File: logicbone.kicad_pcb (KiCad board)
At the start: 8 copper layers, 86.4 x 54.6 mm, 253 parts, among them IC1 ECP5UM-CABGA381, IC10 AT25SL128A, IC11 FAN5362UMP, IC12 74LVC1G07, IC13 TPS51206, IC14 KSZ9031RNXCA, IC15 TC7USB40MU, IC16 NCP349, IC17 NCP110AMX110, IC18 NCP110AMX110, IC19 NCP115AMX250, IC2 DDR3-TFBGA78, IC20 NCP115AMX250, IC3 DDR3-TFBGA78, IC4 MXL7704, IC5 PI6CG18401, IC6 74LVC1G02, IC7 FUSB302-QFN14, IC8 STM32FLxx-QFN48, IC9 ADC120, J1 NGFF-KEY-E, J2 GCT_USB4110_USBC, J3 ARJM11xx-502, J4 FTSH-105-DV-K, J5 Conn_02x05_Odd_Even, J6 Micro_SD_MEM2075, P8 BB_2x23, P9 BB_2x23, Q1 Q_PMOS_GSD, SW1 SW_SPST, SW2 SW_SPST, Y1 25MHz, Y2 32.768kHz

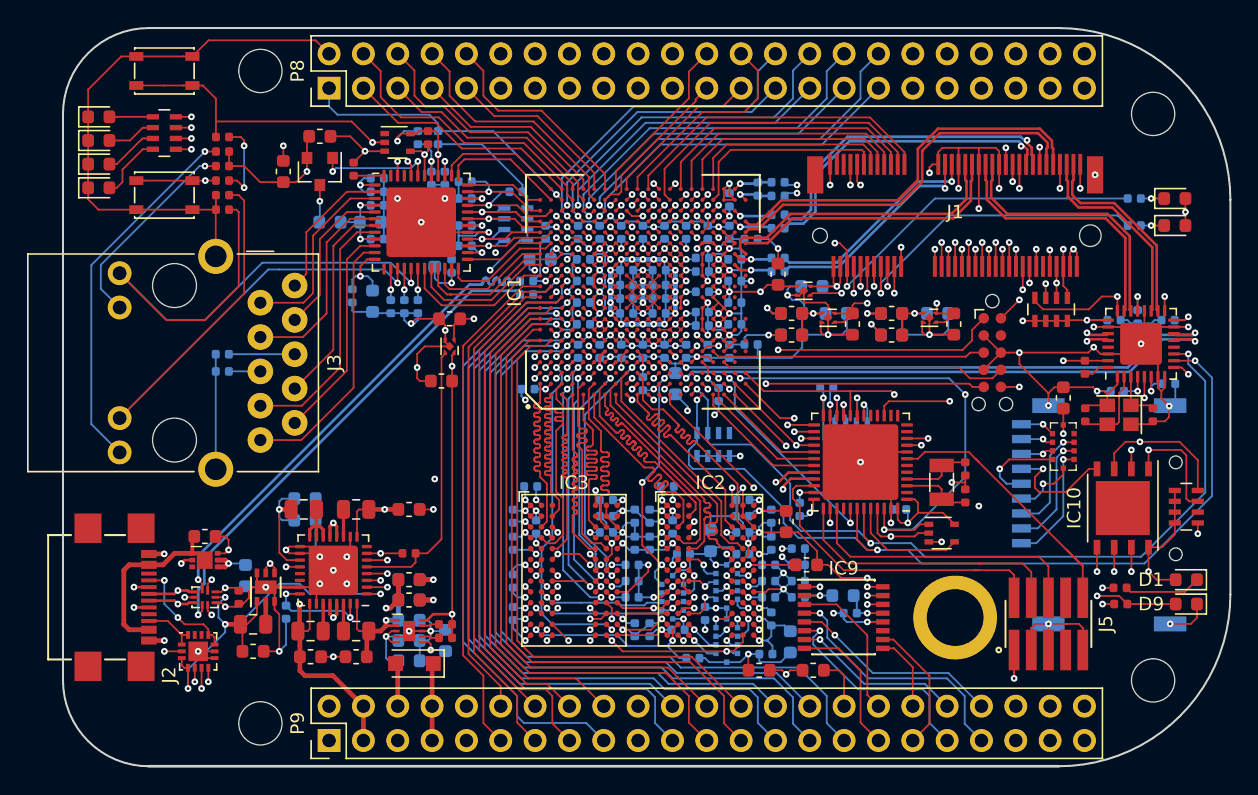
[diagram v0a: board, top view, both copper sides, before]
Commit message: Move +3V3 supply onto PMIC LDO.
The default configuration of the MXL7704 allows the LDO to be used
as an always-on supply by controlling the power-on using SEQ_EN in
place of GLOBAL_EN. Doing so allows us to elminiate another
regulator.
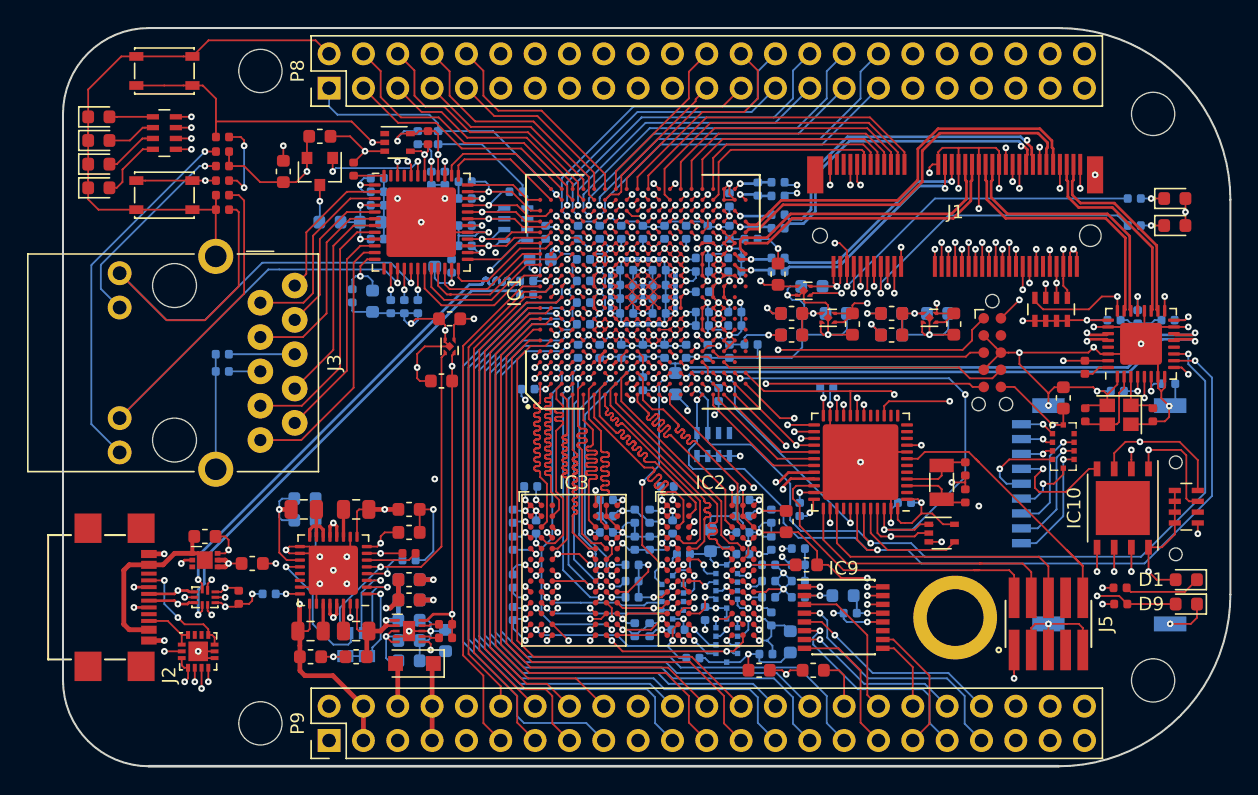
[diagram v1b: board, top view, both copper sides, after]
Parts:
- removed IC11: FAN5362UMP, Package_DFN_QFN:DFN-6-1EP_2x2mm_P0.65mm_EP1x1.6mm
- removed L12: L, Inductor_SMD:L_0805_2012Metric
- added R32: 10k, Resistor_SMD:R_0402_1005Metric, B.Cu at (125.6, 84.8)
- C104: moved to F.Cu
- moved RN8 39.8 mm to (121.7, 91.0)
- moved C100 14.5 mm to (125.6, 82.7)
- moved C107 1.84 mm to (115.2, 87.2), turned to 180 degrees
- moved C104 1.03 mm to (114.0, 85.0), turned to 0 degrees
- moved C517 0.70 mm to (149.7, 66.4)
- moved C516 0.70 mm to (149.7, 63.4)
- moved C103 0.61 mm to (162.2, 80.5)
- moved C252 0.10 mm to (149.7, 67.4)
- moved C258 0.10 mm to (149.7, 62.4)
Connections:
- C280 pad 1: +3V3 -> VCC3V3
- C281 pad 1: +3V3 -> VCC3V3
- D1 pad 2: +3V3 -> VCC3V3
- IC1 pad D10: /Exp Headers/P9_GPIO21 -> /Exp Headers/ADC_SCLK
- IC1 pad D9: /Exp Headers/ADC_SCLK -> /Exp Headers/P9_GPIO21
- IC1 pad P10: +3V3 -> VCC3V3
- IC1 pad P9: +3V3 -> VCC3V3
- IC1 pad T4: +3V3 -> VCC3V3
- IC10 pad 8: +3V3 -> VCC3V3
- IC4 pad 7: +3V3 -> VBUS
- IC4 pad 8: Net-(IC4-Pad8) -> +3V3
- IC8 pad 10: /Supervisor/PMIC_ENABLE -> Net-(IC8-Pad10)
- J4 pad 6: +3V3 -> VCC3V3
- R17 pad 2: +3V3 -> VCC3V3
- R18 pad 1: /FPGA Power/PWR_VCCAUX -> /Supervisor/PMIC_ENABLE
- R18 pad 2: +3V3 -> VBUS
- RN7 pad 5: +3V3 -> VCC3V3
- RN7 pad 6: +3V3 -> VCC3V3
- RN7 pad 7: +3V3 -> VCC3V3
- RN7 pad 8: +3V3 -> VCC3V3
- RN8 pad 1: /Supervisor/PMIC_SDA -> /FPGA Power/PWR_VCCAUX
- RN8 pad 2: /Supervisor/PMIC_SCL -> /Supervisor/PMIC_PGOOD
- RN8 pad 3: /Supervisor/PMIC_PGOOD -> /Supervisor/PMIC_SCL
- RN8 pad 4: /Supervisor/PMIC_SEQ -> /Supervisor/PMIC_SDA
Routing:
- net +3V3: track 245.5 -> 183.8 mm, vias 18 -> 12
- net /Supervisor/PMIC_ENABLE: track 60.3 -> 3.82 mm, vias 2 -> 0
- net VCC3V3: track 371.9 -> 416.4 mm, vias 22 -> 26
- net GND: track 1317.7 -> 1337.2 mm, vias 147 -> 146
- net /Supervisor/PMIC_PGOOD: track 52.3 -> 59.6 mm
- net /FPGA Power/PWR_VCCAUX: track 20.6 -> 26.7 mm, vias 0 -> 1
- net VBUS: track 50.4 -> 54.7 mm
- net /Supervisor/PMIC_SCL: track 52.7 -> 55.8 mm
- net /FPGA Power/VCCA1: track 17.1 -> 19.4 mm
- net /Supervisor/PMIC_SDA: track 51.9 -> 54.2 mm
- net Net-(IC11-Pad2): track 1.70 -> 0.00 mm
- net /FPGA SERDES/VCCTRX1: track 26.1 -> 24.9 mm
- net /Exp Headers/ADC_SCLK: track 40.7 -> 40.3 mm, vias 3 -> 2
- net VCCAUXTRX: track 16.4 -> 16.5 mm, vias 3 -> 4

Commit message: Remove STM32 and plan to use an FPGA bootloader instead.
The MXL7704 is close enough to what the ECP5 needs that we can let
it boot itself from the OTP and then fixup the voltages once the
FPGA bootloader starts (the OTP is correct for the ECP5-5G).
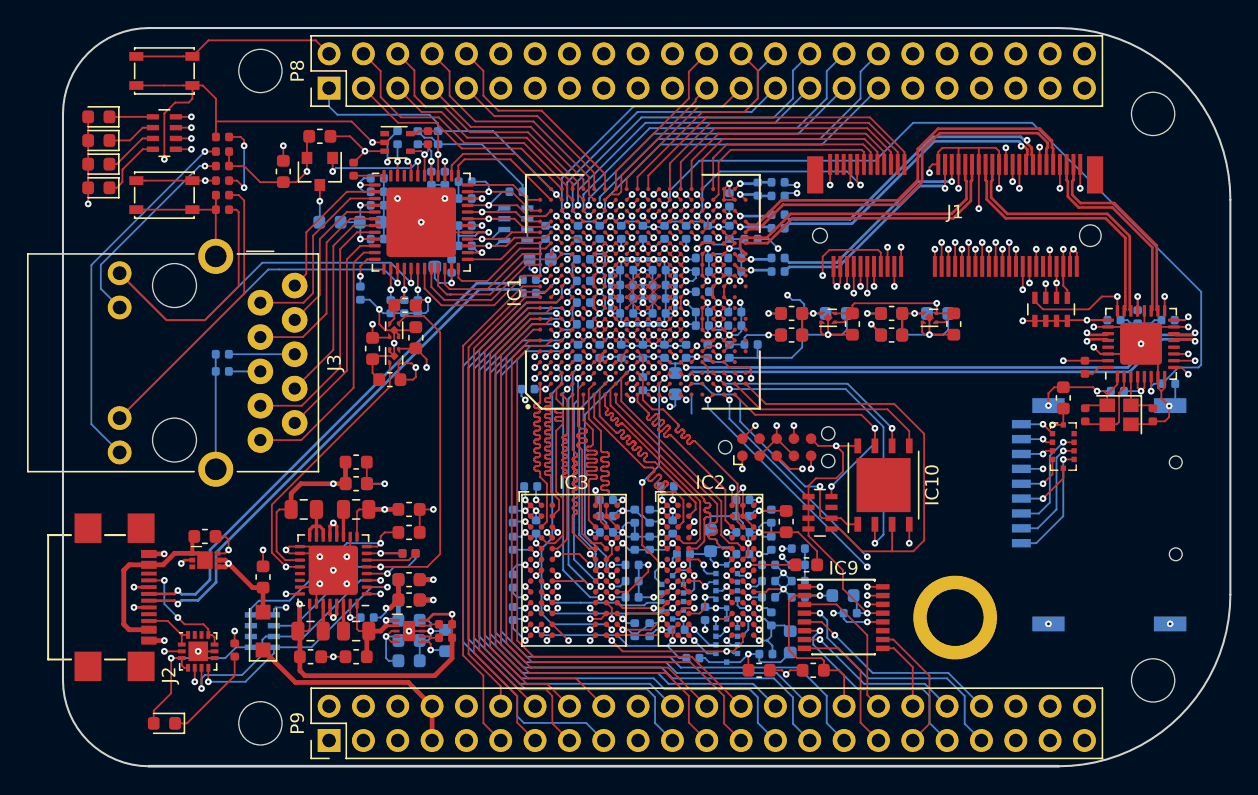
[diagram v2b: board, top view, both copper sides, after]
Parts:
- removed C101, C102, C103, C281: 100nF, Capacitor_SMD:C_0402_1005Metric
- removed C105, C106, C107: C_Small, Capacitor_SMD:C_0402_1005Metric
- removed D7, D8, D9: LED_ALT, LED_SMD:LED_0603_1608Metric
- removed IC15: TC7USB40MU, Package_DFN_QFN:UQFN-10_1.4x1.8mm_P0.4mm
- removed IC6: 74LVC1G02, Package_TO_SOT_SMD:SOT-353_SC-70-5
- removed IC8: STM32FLxx-QFN48, Package_DFN_QFN:QFN-48-1EP_7x7mm_P0.5mm_EP5.6x5.6mm
- removed J5: Conn_02x05_Odd_Even, KiCAD_Magic:ftsh-105-01-dv
- removed R11, R12: 10k, Resistor_SMD:R_0402_1005Metric
- removed R17: 470, Resistor_SMD:R_0402_1005Metric
- removed R34: 4.7k, Resistor_SMD:R_0402_1005Metric
- removed RN8: 4.7k, Resistor_SMD:R_Array_Concave_4x0603
- removed Y2: 32.768kHz, Crystal:Crystal_SMD_3215-2Pin_3.2x1.5mm
- added C1: C_Small, Capacitor_SMD:C_0402_1005Metric, B.Cu at (122.5, 89.0)
- added C2: 100nF, Capacitor_SMD:C_0402_1005Metric, B.Cu at (124.8, 53.5)
- C152, C161, C304, R32: moved to F.Cu
- J4: value FTSH-105-DV-K -> TC2050-IDC-NL
- R18: moved to B.Cu
- moved D1 76.3 mm to (107.5, 96.8)
- moved R10 65.7 mm to (112.7, 91.4), turned to 270 degrees
- moved RN5 36.1 mm to (114.8, 90.0), turned to 180 degrees
- moved C161 32.0 mm to (124.2, 71.4)
- moved C167 30.5 mm to (122.9, 69.1), turned to 270 degrees
- moved IC19 30.4 mm to (124.5, 67.8), turned to 90 degrees
- moved RN7 27.1 mm to (156.0, 81.2)
- moved IC10 17.8 mm to (160.7, 79.2), turned to 90 degrees
- moved J4 17.4 mm to (152.8, 76.4), turned to 0 degrees
- moved D6 11.5 mm to (114.8, 90.0), turned to 90 degrees
- moved C162 9.88 mm to (121.7, 79.1), turned to 0 degrees
- moved C280 7.69 mm to (147.3, 64.9), turned to 0 degrees
- moved C151 4.66 mm to (121.7, 79.1)
- moved C152 4.65 mm to (121.7, 77.5)
- moved IC20 4.16 mm to (124.5, 69.7)
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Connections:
- net /FPGA SERDES/M2_USB_DM renamed /FPGA SERDES/M2_USB-
- net /FPGA SERDES/M2_USB_DP renamed /FPGA SERDES/M2_USB+
- net /Supervisor/FLASH_MISO renamed /FPGA Programming/FLASH_MISO
- net /Supervisor/FLASH_MOSI renamed /FPGA Programming/FLASH_MOSI
- net /Supervisor/FLASH_SCLK renamed /FPGA Programming/FLASH_SCLK
- net /Supervisor/FPGA_TCK renamed /FPGA Programming/FPGA_TCK
- net /Supervisor/FPGA_TDI renamed /FPGA Programming/FPGA_TDI
- net /Supervisor/FPGA_TDO renamed /FPGA Programming/FPGA_TDO
- net /Supervisor/FPGA_TMS renamed /FPGA Programming/FPGA_TMS
- net /Supervisor/USB_CC1 renamed /FPGA Programming/USB_CC1
- net /Supervisor/USB_CC2 renamed /FPGA Programming/USB_CC2
- net /Supervisor/~FPGA_INIT renamed /FPGA Programming/~FPGA_INIT
- C162 pad 1: VCC3V3 -> VCORE
- D1 pad 2: VCC3V3 -> +3V3
- D2 pad 1: GND -> Net-(D2-Pad1)
- D2 pad 2: Net-(D2-Pad2) -> VCC3V3
- D3 pad 1: GND -> Net-(D3-Pad1)
- D3 pad 2: Net-(D3-Pad2) -> VCC3V3
- D4 pad 1: GND -> Net-(D4-Pad1)
- D4 pad 2: Net-(D4-Pad2) -> VCC3V3
- D5 pad 1: GND -> Net-(D5-Pad1)
- D5 pad 2: Net-(D5-Pad2) -> VCC3V3
- IC1 pad D13: /Ethernet/MMC_DAT0 -> /Ethernet/MMC_DAT2
- IC1 pad E13: /Ethernet/MMC_DAT2 -> /Ethernet/MMC_DAT0
- IC1 pad E14: /Ethernet/MMC_DET -> /Ethernet/MMC_CMD
- IC1 pad E15: /Ethernet/MMC_CMD -> /Ethernet/MMC_DET
- IC1 pad L16: /FPGA SERDES/~M2_WDIS2 -> /FPGA SERDES/M2_SUSCLK
- IC1 pad L17: /FPGA SERDES/~PCIE_RESET0 -> /FPGA SERDES/~M2_WDIS2
- IC1 pad L18: /FPGA SERDES/~PCIE_RESET1 -> /FPGA SERDES/~PCIE_WAKE0
- IC1 pad M18: /FPGA SERDES/M2_SUSCLK -> /FPGA SERDES/~PCIE_RESET0
- IC1 pad M19: /FPGA SERDES/~PCIE_WAKE0 -> /Ethernet/25M_REFCLK
- IC1 pad N1: /FPGA Memory/~DDR3_RST -> Net-(IC1-PadN1)
- IC1 pad N17: /FPGA SERDES/M2_COEX2 -> /FPGA SERDES/M2_COEX3
- IC1 pad N18: /FPGA SERDES/M2_VEND1 -> /FPGA SERDES/M2_VEND2
- IC1 pad N19: /FPGA SERDES/~M2_SDIO_WAKE -> /FPGA SERDES/~PCIE_RESET1
- IC1 pad N20: /FPGA SERDES/M2_COEX3 -> /FPGA SERDES/~M2_SDIO_WAKE
- IC1 pad P1: Net-(IC1-PadP1) -> /FPGA Memory/~DDR3_RST
- IC1 pad P18: /FPGA SERDES/M2_COEX1 -> /FPGA SERDES/M2_COEX2
- IC1 pad P19: /FPGA SERDES/M2_VEND2 -> /FPGA SERDES/M2_VEND1
- IC1 pad R1: /Exp Headers/SDA -> Net-(IC1-PadR1)
- IC1 pad R16: /FPGA SERDES/M2_TXD -> Net-(IC1-PadR16)
- IC1 pad R17: /FPGA SERDES/M2_RXD -> /FPGA SERDES/M2_TXD
- IC1 pad R2: /Supervisor/~FLASH_CSEL -> /FPGA Programming/~FLASH_CSEL
- IC1 pad R3: /Supervisor/USB_SEL -> /FPGA Programming/~USB_INT
- IC1 pad T1: /Exp Headers/SCL -> Net-(IC1-PadT1)
- IC1 pad T19: /FPGA SERDES/M2_VEND0 -> /FPGA SERDES/M2_COEX1
- IC1 pad T2: /Exp Headers/PWR_BUTTON -> Net-(IC1-PadT2)
- IC1 pad U1: /Supervisor/FPGA_UART_RXD -> /Exp Headers/SCL
- IC1 pad U17: /FPGA SERDES/M2_LED1 -> /FPGA SERDES/M2_RXD
- IC1 pad U18: /FPGA SERDES/M2_LED2 -> /FPGA SERDES/M2_VEND0
- IC1 pad U2: /Supervisor/FPGA_UART_TXD -> /Exp Headers/PWR_BUTTON
- IC1 pad V1: /Supervisor/FPGA_UART_CLK -> /Exp Headers/SDA
- IC1 pad W1: /Supervisor/FLASH_D3 -> /FPGA Programming/FLASH_D3
- IC1 pad Y2: /Supervisor/FLASH_D2 -> /FPGA Programming/FLASH_D2
- IC1 pad Y3: /Supervisor/FPGA_DONE -> /FPGA Programming/FPGA_DONE
- IC10 pad 1: /Supervisor/~FLASH_CSEL -> /FPGA Programming/~FLASH_CSEL
- IC10 pad 3: /Supervisor/FLASH_D2 -> /FPGA Programming/FLASH_D2
- IC10 pad 7: /Supervisor/FLASH_D3 -> /FPGA Programming/FLASH_D3
- IC14 pad 46: /Ethernet/25M_REFCLK -> Net-(C2-Pad2)
- IC19 pad 3: /FPGA Power/PWR_SERDES -> /FPGA Power/PMIC_PG1
- IC20 pad 3: /FPGA Power/PWR_VCCAUX -> /FPGA Power/PMIC_PG2
- IC4 pad 2: /Supervisor/PMIC_SDA -> /Exp Headers/SDA
- IC4 pad 20: /Supervisor/PMIC_PGOOD -> /FPGA Power/PMIC_PG2
- IC4 pad 3: /Supervisor/PMIC_SCL -> /Exp Headers/SCL
- IC4 pad 4: /Supervisor/PMIC_SEQ -> /FPGA Power/PMIC_SEQ
- IC4 pad 5: /FPGA Power/PWR_VCCAUX -> /FPGA Power/PMIC_PG1
- IC4 pad 6: /Supervisor/PMIC_ENABLE -> /FPGA Power/PMIC_ENABLE
- IC5 pad 5: VCC3V3 -> VCC1V8
- IC7 pad 5: /Supervisor/~USB_INT -> /FPGA Programming/~USB_INT
- J1 pad 16: /FPGA SERDES/M2_LED2 -> /Ethernet/LED_USER2
- J1 pad 6: /FPGA SERDES/M2_LED1 -> /Ethernet/LED_USER1
- J2 pad A6: /Supervisor/USB_D+ -> /Ethernet/FPGA_USB+
- J2 pad A7: /Supervisor/USB_D- -> /Ethernet/FPGA_USB-
- J2 pad B6: /Supervisor/USB_D+ -> /Ethernet/FPGA_USB+
- J2 pad B7: /Supervisor/USB_D- -> /Ethernet/FPGA_USB-
- R1 pad 1: Net-(IC1-PadB12) -> /Ethernet/FPGA_USB+
- R1 pad 2: /Ethernet/FPGA_USB+ -> Net-(IC1-PadB12)
- R18 pad 1: /Supervisor/PMIC_ENABLE -> VBUS
- R18 pad 2: VBUS -> /FPGA Power/PMIC_SEQ
- R2 pad 1: Net-(IC1-PadC12) -> /Ethernet/FPGA_USB-
- R2 pad 2: /Ethernet/FPGA_USB- -> Net-(IC1-PadC12)
- R32 pad 1: GND -> /FPGA Power/PMIC_ENABLE
- R32 pad 2: /Supervisor/PMIC_SEQ -> VBUS
- RN5 pad 1: /Exp Headers/SCL -> /FPGA Power/PMIC_PG2
- RN5 pad 2: /Exp Headers/SDA -> /FPGA Power/PMIC_PG1
- RN5 pad 3: Net-(RN5-Pad3) -> /Exp Headers/SCL
- RN5 pad 4: Net-(RN5-Pad4) -> /Exp Headers/SDA
- RN7 pad 1: /Supervisor/FLASH_D3 -> /FPGA Programming/FLASH_D2
- RN7 pad 2: Net-(RN7-Pad2) -> /FPGA Programming/~FLASH_CSEL
- RN7 pad 3: /Supervisor/~FLASH_CSEL -> Net-(RN7-Pad3)
- RN7 pad 4: /Supervisor/FLASH_D2 -> /FPGA Programming/FLASH_D3
- RN9 pad 1: Net-(D2-Pad2) -> Net-(D2-Pad1)
- RN9 pad 2: Net-(D3-Pad2) -> Net-(D3-Pad1)
- RN9 pad 3: Net-(D4-Pad2) -> Net-(D4-Pad1)
- RN9 pad 4: Net-(D5-Pad2) -> Net-(D5-Pad1)
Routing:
- net GND: track 1337.2 -> 1121.2 mm, vias 146 -> 137
- net +3V3: track 183.8 -> 72.9 mm, vias 12 -> 5
- net /FPGA Programming/~USB_INT: track 0.00 -> 69.1 mm, vias 0 -> 2
- net /Supervisor/STM_USB-: track 64.1 -> 0.00 mm, vias 2 -> 0
- net /Supervisor/STM_USB+: track 64.0 -> 0.00 mm, vias 2 -> 0
- net /Supervisor/PMIC_PGOOD: track 59.6 -> 0.00 mm, vias 3 -> 0
- net /Supervisor/~USB_INT: track 57.4 -> 0.00 mm, vias 2 -> 0
- net /Supervisor/PMIC_SCL: track 55.8 -> 0.00 mm, vias 2 -> 0
- net /Supervisor/PMIC_SEQ: track 55.2 -> 0.00 mm, vias 2 -> 0
- net /Supervisor/PMIC_SDA: track 54.2 -> 0.00 mm, vias 2 -> 0
- net /Supervisor/USB_SEL: track 51.9 -> 0.00 mm, vias 2 -> 0
- net /Supervisor/~FLASH_CSEL: track 51.1 -> 0.00 mm, vias 3 -> 0
- net /Supervisor/FLASH_D2: track 44.0 -> 0.00 mm, vias 2 -> 0
- net /Supervisor/FLASH_D3: track 44.0 -> 0.00 mm, vias 3 -> 0
- net /Supervisor/FPGA_DONE: track 43.2 -> 0.00 mm, vias 2 -> 0
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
